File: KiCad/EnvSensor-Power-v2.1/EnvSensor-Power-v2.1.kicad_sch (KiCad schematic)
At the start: 141 parts, among them J1 USB_B_Micro, J2 USB_C_Receptacle_USB2.0, J3 BattSense, J4 Conn_01x02, J5 Conn_01x02, J6 POWER_OUTPUT, Q1 AO6804A, Q2 IRLML2244, Q3 ZXMP6A16K, SW1 BATT_SWITCH, SW2 Start, U1 LTC3440, U2 AP9101CK, U3 MCP1825S-3.3, U4 TPS631000, U5 MCP73843-4.2, U6 MCP1826S-5.0, U7 LTC4052, U8 LM2735XMF

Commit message: Finishing touches
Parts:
- removed Q2: IRLML2244, Package_TO_SOT_SMD:SOT-23, symbol Device:Q_PMOS_GSD
- removed R18: 3k3, Resistor_SMD:R_0805_2012Metric, symbol Device:R
- D4: value POWER LED -> CHARGE LED (Red)
- D5: value POWER LED -> POWER LED (Red)
- J2: footprint Connector_USB:USB_C_Receptacle_HRO_TYPE-C-31-M-12 -> Connector_USB:USB_C_Receptacle_GCT_USB4135-GF-A_6P_TopMnt_Horizontal
- J4: value Conn_01x02 -> 3V3 Sense
- J5: value Conn_01x02 -> 5V Sense
- L2: value 100-600 -> 100-600R
- SW1: footprint Button_Switch_THT:SW_Tactile_SPST_Angled_PTS645Vx31-2LFS -> Button_Switch_THT:SW_Lever_1P2T_NKK_GW12LxH; symbol Switch:SW_SPST -> Switch:SW_SPDT
- TP1, TP2, TP3, TP4, TP5, TP6, TS1, TS2, TS3, TS4, TS5, TS6, TS7: footprint TestPoint:TestPoint_Pad_D1.5mm -> TestPoint:TestPoint_THTPad_D1.5mm_Drill0.7mm
- U2: value AP9101CK -> AP9101CK6; footprint Package_TO_SOT_SMD:SOT-23-5 -> Package_TO_SOT_SMD:SOT-23-6; symbol Battery_Management:AP9101CK -> Battery_Management:AP9101CK6
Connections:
- net L_CHRG_POWER is gone; now on net VBUS: C18.1, R15.2, R22.2, U5.2 (VDD)
- net -BATT: now also U2.6 (VSS); no longer U2.3 (VSS)
- net BATT_SW: now also SW1.3 (C); no longer SW1.1 (A)
- net PROT_VDD: now also U2.5 (VDD); no longer U2.2 (VDD)
- net PROT_DO: now reaches U2.1 (DO)
- net PROT_DO: now also Q1.4 (G2); no longer R9.1
- net at U2.4 (NC): no longer Q1.4 (G2)
- net PROT_CO: now reaches Q1.6 (G2)
- net PROT_CO: now also U2.3 (CO); no longer U2.5 (CO)
- net 3V3_NOT_REG renamed 3V7_NOT_REG
- net 5V_FILTERED renamed 5V5_FILTERED
- net 5V_NOT_REG renamed 5V5_NOT_REG
- new net PROT_VM: R9.1, U2.2 (VM)
- no-connect marks 7 -> 10
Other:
- note added: "10n-1u/100n typ"
- note added: "3.3V Buck-Boost DC/DC Converter with LTC3440"
- note added: "300R-4k/2k7 typ"
- note added: "330R-470R"
- note added: "AO6804A Rds(on): 30mR @ Vgs=2.5V 23mR @ Vgs=4.5V"
- note added: "AP9101CK-AHTRG1 (SOT25) Vcu=4.425V Vdl=2.5V Vdoc=75mV Vcoc=-75mV AP9101CK6-AYTRG1 (SOT26) Vcu=4.275V Vdl=2.8V Vdoc=150mV Vcoc=-100mV"
- note added: "Charging limit: Vcoc/(2*Rds(on))=75mV/23mR=3.7A"
- note added: "NCR18650B 2.5V - 4.2V"
- note added: "Vreg: 4.137-4.242"
- note added: "Vreg: 4.179-4.221"
- note removed: "3.3V Buck-Boost DC/DC Converter"
- note removed: "AP9101CK-AHTRG1 Vcu=4.425V Vdl=2.5V Vdoc=75mV Vcoc=-75mV"

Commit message: LM2735 fixes
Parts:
- C2, C29, C30: footprint Capacitor_SMD:C_1206_3216Metric -> Capacitor_SMD:C_0805_2012Metric
- C28: value 1n8 -> 1n
- L4: footprint Inductor_SMD:L_TDK_SLF10145 -> Inductor_SMD:L_1210_3225Metric
- L5: value SLF7045T-3R3M2R5-PF / 3u3 -> MSS5131-473MLC / 47u; footprint Inductor_SMD:L_TDK_SLF7045 -> Inductor_SMD:L_Coilcraft_XAL5030-XXX
- R32: value 1M -> 300k
- U8: value LM2735XMF -> LM2735YMF
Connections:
- net BATT_BARE: now also SW1.3 (C); no longer SW1.2 (B)
- net BATT_SW: now also SW1.2 (B); no longer SW1.3 (C)
- no-connect marks 10 -> 11
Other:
- note added: "L=1u Isat 2-4.3A DCR 40-140mR"
- note added: "LM2735X f=1.6MHz LM2735Y f=520kHz"
- note added: "MMZ2012S601AT000"
- note added: "Ripple 10%, Imax=250mA: L: 47uH IDC: 0.3A"
- note added: "Rosc=60k fosc=1MHz Rosc=120k fosc=500kHz"
- note added: "f=2.2MHz"
- note removed: "L: 2.2-4.3uH DCR: - 450mOhm IDC: 2.3-3.0A"
- note removed: "Rosc=60k fosc=1MHz"
- moved on the sheet: R32, SW1

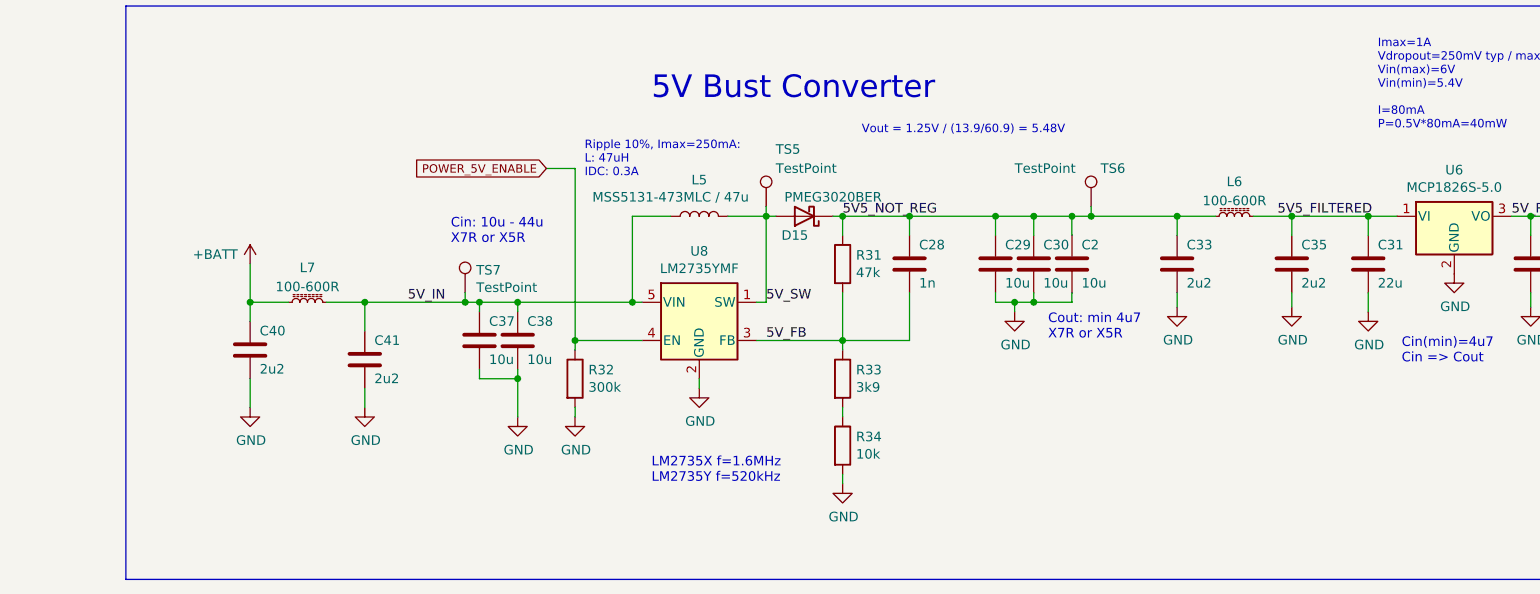
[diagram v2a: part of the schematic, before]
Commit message: LM2735 fixes
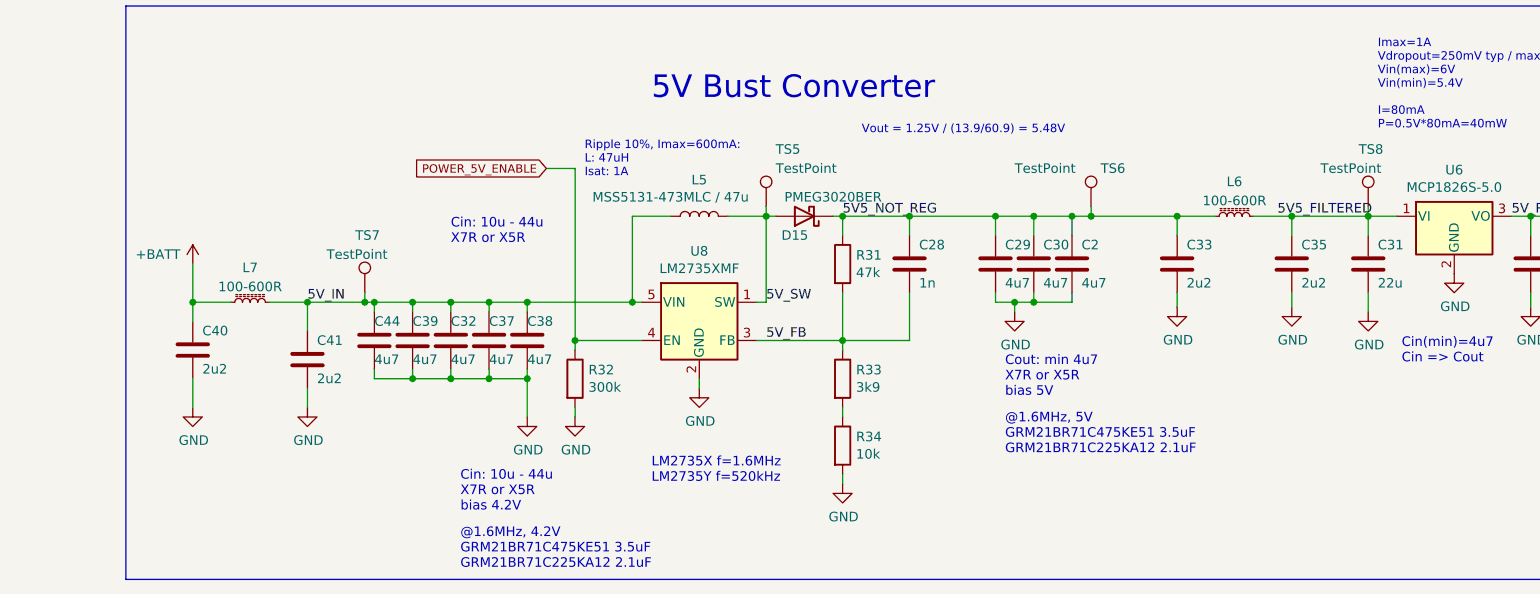
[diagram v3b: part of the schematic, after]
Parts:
- added C32, C39, C44: 4u7, Capacitor_SMD:C_0805_2012Metric, symbol Device:C
- added TS8: TestPoint, TestPoint:TestPoint_THTPad_D1.5mm_Drill0.7mm, symbol Connector:TestPoint
- C2, C29, C30, C37, C38: value 10u -> 4u7
- U8: value LM2735YMF -> LM2735XMF
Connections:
- net 5V5_FILTERED: now also TS8.1
- net 5V_IN: now also C32.1, C39.1, C44.1
- net GND: now also C32.2, C39.2, C44.2
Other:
- note added: "@1.6MHz, 4.2V GRM21BR71C475KE51 3.5uF GRM21BR71C225KA12 2.1uF"
- note added: "@1.6MHz, 5V GRM21BR71C475KE51 3.5uF GRM21BR71C225KA12 2.1uF"
- note added: "Cin: 10u - 44u X7R or X5R bias 4.2V"
- note added: "Cout: min 4u7 X7R or X5R bias 5V"
- note added: "Ripple 10%, Imax=600mA: L: 47uH Isat: 1A"
- note removed: "Cout: min 4u7 X7R or X5R"
- note removed: "Ripple 10%, Imax=250mA: L: 47uH IDC: 0.3A"
- moved on the sheet: C37, C38, C40, C41, L7, TS7

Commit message: Fixes
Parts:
- removed C44: 4u7, Capacitor_SMD:C_0805_2012Metric, symbol Device:C
- added C33, C5, C7: 4u7, Capacitor_SMD:C_0805_2012Metric, symbol Device:C
- C10, C8, C9: value 10u -> 4u7
- C2: renamed from C3; value 22u -> 4u7; footprint Capacitor_SMD:C_1206_3216Metric -> Capacitor_SMD:C_0805_2012Metric
- C3: renamed from C4; value 22u -> 4u7; footprint Capacitor_SMD:C_1206_3216Metric -> Capacitor_SMD:C_0805_2012Metric
- C4: renamed from C5; value 22u -> 4u7; footprint Capacitor_SMD:C_1206_3216Metric -> Capacitor_SMD:C_0805_2012Metric
- L1: value SLF10145T-220M1R9-H / 22u -> MSS7341-473MLD / 47u; footprint Inductor_SMD:L_TDK_SLF10145 -> Inductor_SMD:L_Coilcraft_XAL8080-XXX
- L5: value MSS5131-473MLC / 47u -> MSS7341-473MLD / 47u; footprint Inductor_SMD:L_Coilcraft_XAL5030-XXX -> Inductor_SMD:L_Coilcraft_XAL8080-XXX
- renumbered C6 to C15, C15 to C16, C16 to C17, C17 to C18, C18 to C19, C19 to C20, C20 to C21, C21 to C22, C22 to C23, C23 to C24, C24 to C25, C25 to C26, C26 to C27, C27 to C28, C28 to C29, C29 to C30, C30 to C31, C2 to C32, C33 to C34, C31 to C36, C34 to C37, C36 to C38, C32 to C40, C37 to C41, C38 to C42, C40 to C43, C41 to C44, C43 to C45, C42 to C46, C7 to C6, D15 to D10, D5 to D4, D6 to D5, D4 to D6, D13 to D8, D14 to D9, JP8 to JP7, JP9 to JP8, JP7 to JP9, Q3 to Q2, R20 to R18, R22 to R20, R23 to R21, R24 to R22, R25 to R23, R26 to R24, R21 to R25, R29 to R26, R30 to R27, R31 to R28, R32 to R29, R33 to R30, R34 to R31, TS8 to TS7, TS7 to TS8
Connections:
- net 3V7_NOT_REG: now also C5.1
- net 5V5_NOT_REG: now also C33.1
- net BATT_3V3_FILTER: now also C7.1
- net GND: now also C33.2, C5.2, C7.2
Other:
- note added: "Cin min 4.7uF"
- note removed: "Cin: 10u - 44u X7R or X5R"
- moved on the sheet: C3, C4

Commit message: More fixes
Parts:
- added TS5: TestPoint, TestPoint:TestPoint_THTPad_D1.5mm_Drill0.7mm, symbol Connector:TestPoint
- L1, L5: footprint Inductor_SMD:L_Coilcraft_XAL8080-XXX -> Inductor_SMD:L_Coilcraft_XAL7050-XXX
- renumbered TS5 to TS6, TS6 to TS7, TS7 to TS8, TS8 to TS9
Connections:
- net 3V3_FILTER: now also TS5.1
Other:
- note added: "AP9101CK-AHTRG1 (SOT25) Vcu=4.425V Vdl=2.5V Vdoc=75mV Vcoc=-75mV AP9101CK6-AYTRG1 (SOT26) Vcu=4.275V Vdl=2.8V Vdoc=150mV Vcoc=-100mV AP9101CK6-AXTRG1 (SOT26) Vcu=4.28V Vdl=2.8V Vdoc=150mV Vcoc=-100mV"
- note removed: "AP9101CK-AHTRG1 (SOT25) Vcu=4.425V Vdl=2.5V Vdoc=75mV Vcoc=-75mV AP9101CK6-AYTRG1 (SOT26) Vcu=4.275V Vdl=2.8V Vdoc=150mV Vcoc=-100mV"
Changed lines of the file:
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@@
   (junction (at 314.96 293.37) (diameter 0) (color 0 0 0 0)
   )
+  (junction (at 485.14 179.07) (diameter 0) (color 0 0 0 0)
+  )
   (junction (at 438.15 281.94) (diameter 0) (color 0 0 0 0)
   )
@@
     (stroke (width 0) (type default))
   )
+  (wire (pts (xy 485.14 179.07) (xy 493.395 179.07))
+    (stroke (width 0) (type default))
+  )
   (wire (pts (xy 351.79 208.28) (xy 358.14 208.28))
     (stroke (width 0) (type default))
@@
     (stroke (width 0) (type default))
   )
+  (wire (pts (xy 485.14 177.8) (xy 485.14 179.07))
+    (stroke (width 0) (type default))
+  )
   (wire (pts (xy 193.04 274.955) (xy 193.04 277.495))
     (stroke (width 0) (type default))
@@
     (stroke (width 0) (type default))
   )
-  (wire (pts (xy 481.965 179.07) (xy 493.395 179.07))
+  (wire (pts (xy 481.965 179.07) (xy 485.14 179.07))
     (stroke (width 0) (type default))
   )
@@
     (effects (font (size 1.1176 1.1176)) (justify left bottom))
   )
-  (text "AP9101CK-AHTRG1 (SOT25)\nVcu=4.425V Vdl=2.5V Vdoc=75mV  Vcoc=-75mV\n\nAP9101CK6-AYTRG1 (SOT26)\nVcu=4.275V Vdl=2.8V Vdoc=150mV Vcoc=-100mV"
-    (at 119.38 117.475 0)
+  (text "AP9101CK-AHTRG1 (SOT25)\nVcu=4.425V Vdl=2.5V Vdoc=75mV  Vcoc=-75mV\n\nAP9101CK6-AYTRG1 (SOT26)\nVcu=4.275V Vdl=2.8V Vdoc=150mV Vcoc=-100mV\n\nAP9101CK6-AXTRG1 (SOT26)\nVcu=4.28V Vdl=2.8V Vdoc=150mV Vcoc=-100mV"
+    (at 119.38 121.92 0)
     (effects (font (size 1.27 1.27)) (justify left bottom))
   )
@@
   )
   (text "Imax=500mA\n\nI=110mA | 250mA\nP=0.4V*110mA | 0.4V*250mA\nP=44mW | 100mW "
-    (at 485.14 171.45 0)
+    (at 488.95 168.91 0)
     (effects (font (size 1.1176 1.1176)) (justify left bottom))
   )
@@
   )
   (text "Vdropout = 210mV typ / 350mV max\nVin(min)=3.3V + 0.35V=3.65V"
-    (at 485.14 160.02 0)
+    (at 488.95 158.75 0)
     (effects (font (size 1.27 1.27)) (justify left bottom))
   )
@@
       (effects (font (size 1.27 1.27)))
     )
-    (property "Footprint" "Inductor_SMD:L_Coilcraft_XAL8080-XXX" (at 323.85 281.94 0)
+    (property "Footprint" "Inductor_SMD:L_Coilcraft_XAL7050-XXX" (at 323.85 281.94 0)
       (effects (font (size 1.27 1.27)) hide)
     )
@@
       (effects (font (size 1.27 1.27)))
     )
-    (property "Footprint" "Inductor_SMD:L_Coilcraft_XAL8080-XXX" (at 365.76 129.54 0)
+    (property "Footprint" "Inductor_SMD:L_Coilcraft_XAL7050-XXX" (at 365.76 129.54 0)
       (effects (font (size 1.27 1.27)) hide)
     )
@@
   (symbol (lib_id "Connector:TestPoint") (at 279.4 292.1 0) (unit 1)
     (in_bom yes) (on_board yes) (dnp no)
-    (property "Reference" "TS8" (at 278.13 284.48 0)
+    (property "Reference" "TS9" (at 278.13 284.48 0)
       (effects (font (size 1.27 1.27)) (justify left))
     )
@@
       (project "EnvSensor-Power-v2.1"
         (path "/75844dd9-c348-4927-8288-77f5f5861fbe"
-          (reference "TS8") (unit 1)
+          (reference "TS9") (unit 1)
         )
       )
@@
   (symbol (lib_id "Connector:TestPoint") (at 332.74 280.67 0) (unit 1)
     (in_bom yes) (on_board yes) (dnp no)
-    (property "Reference" "TS5" (at 334.01 273.05 0)
+    (property "Reference" "TS6" (at 334.01 273.05 0)
       (effects (font (size 1.27 1.27)) (justify left))
     )
@@
       (project "EnvSensor-Power-v2.1"
         (path "/75844dd9-c348-4927-8288-77f5f5861fbe"
-          (reference "TS5") (unit 1)
+          (reference "TS6") (unit 1)
         )
       )
@@
   (symbol (lib_id "Connector:TestPoint") (at 375.92 280.67 0) (unit 1)
     (in_bom yes) (on_board yes) (dnp no)
-    (property "Reference" "TS6" (at 377.19 275.59 0)
+    (property "Reference" "TS7" (at 377.19 275.59 0)
       (effects (font (size 1.27 1.27)) (justify left))
     )
@@
       (project "EnvSensor-Power-v2.1"
         (path "/75844dd9-c348-4927-8288-77f5f5861fbe"
-          (reference "TS6") (unit 1)
+          (reference "TS7") (unit 1)
         )
       )
@@
   (symbol (lib_id "Connector:TestPoint") (at 412.75 280.67 0) (unit 1)
     (in_bom yes) (on_board yes) (dnp no)
-    (property "Reference" "TS7" (at 411.48 273.05 0)
+    (property "Reference" "TS8" (at 411.48 273.05 0)
       (effects (font (size 1.27 1.27)) (justify left))
     )
@@
       (project "EnvSensor-Power-v2.1"
         (path "/75844dd9-c348-4927-8288-77f5f5861fbe"
-          (reference "TS7") (unit 1)
+          (reference "TS8") (unit 1)
         )
       )
@@
         )
       )
+    )
+  )
+  (symbol (lib_id "Connector:TestPoint") (at 485.14 177.8 0) (unit 1)
+    (in_bom yes) (on_board yes) (dnp no)
+    (property "Reference" "TS5" (at 483.87 170.18 0)
+      (effects (font (size 1.27 1.27)) (justify left))
+    )
+    (property "Value" "TestPoint" (at 478.79 172.72 0)
+      (effects (font (size 1.27 1.27)) (justify left))
+    )
+    (property "Footprint" "TestPoint:TestPoint_THTPad_D1.5mm_Drill0.7mm" (at 490.22 177.8 0)
+      (effects (font (size 1.27 1.27)) hide)
+    )
+    (property "Datasheet" "~" (at 490.22 177.8 0)
+      (effects (font (size 1.27 1.27)) hide)
+    )
+    (pin "1")
+    (instances
+      (project "EnvSensor-Power-v2.1"
+        (path "/75844dd9-c348-4927-8288-77f5f5861fbe"
+          (reference "TS5") (unit 1)
+        )
+      )

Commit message: More fixes
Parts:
- D1: footprint Diode_SMD:D_SOD-323 -> Diode_SMD:D_SOD-323_HandSoldering
- L1, L5: footprint Inductor_SMD:L_Coilcraft_XAL7050-XXX -> Inductor_SMD:L_Bourns-SRN8040_8x8.15mm
- L4: footprint Inductor_SMD:L_1210_3225Metric -> Inductor_SMD:L_0805_2012Metric
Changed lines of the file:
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@@
       (effects (font (size 1.27 1.27)))
     )
-    (property "Footprint" "Inductor_SMD:L_Coilcraft_XAL7050-XXX" (at 323.85 281.94 0)
+    (property "Footprint" "Inductor_SMD:L_Bourns-SRN8040_8x8.15mm" (at 323.85 281.94 0)
       (effects (font (size 1.27 1.27)) hide)
     )
@@
       (effects (font (size 1.27 1.27)))
     )
-    (property "Footprint" "Inductor_SMD:L_Coilcraft_XAL7050-XXX" (at 365.76 129.54 0)
+    (property "Footprint" "Inductor_SMD:L_Bourns-SRN8040_8x8.15mm" (at 365.76 129.54 0)
       (effects (font (size 1.27 1.27)) hide)
     )
@@
       (effects (font (size 1.27 1.27)))
     )
-    (property "Footprint" "Inductor_SMD:L_1210_3225Metric" (at 369.57 198.12 0)
+    (property "Footprint" "Inductor_SMD:L_0805_2012Metric" (at 369.57 198.12 0)
       (effects (font (size 1.27 1.27)) hide)
     )
@@
       (effects (font (size 1.27 1.27)) (justify right))
     )
-    (property "Footprint" "Diode_SMD:D_SOD-323" (at 82.55 46.99 0)
+    (property "Footprint" "Diode_SMD:D_SOD-323_HandSoldering" (at 82.55 46.99 0)
       (effects (font (size 1.27 1.27)) hide)
     )
